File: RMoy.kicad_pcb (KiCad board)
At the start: 2 copper layers, 89 x 54 mm, 21 parts, among them J1 AudioJack3_SwitchTR, J2 AudioJack3_SwitchTR, J3 Jack-DC, U1 OPA2134

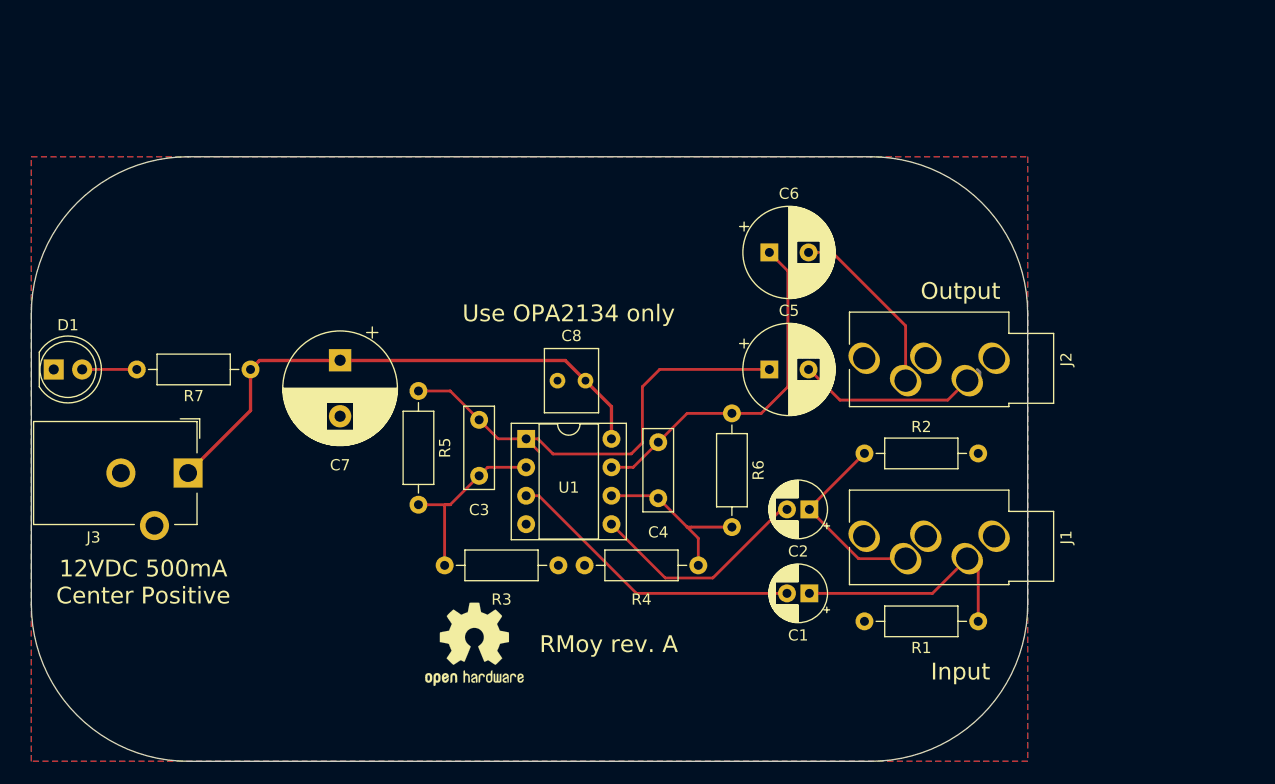
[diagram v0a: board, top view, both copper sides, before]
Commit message: PCB is reworked
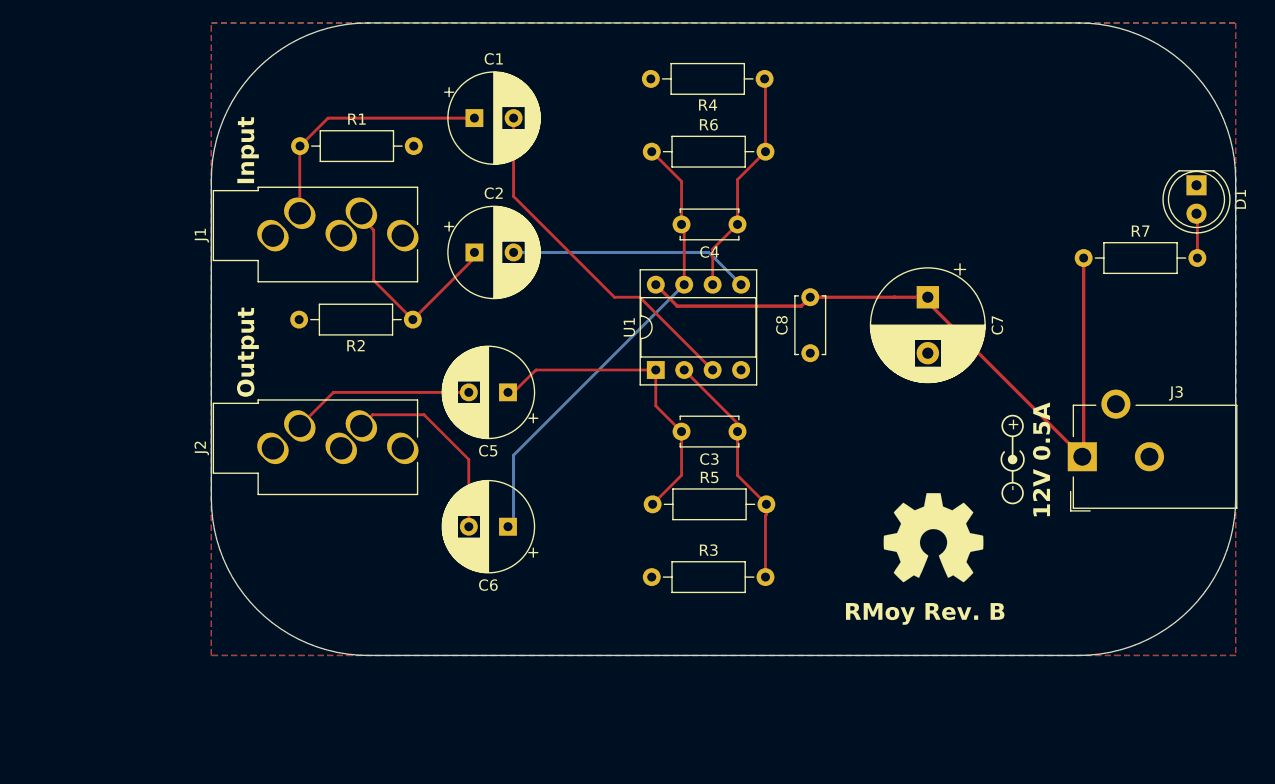
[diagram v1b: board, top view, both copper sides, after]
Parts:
- removed the REF** at (136.0, 109.0)
- added REF**: Symbol_Barrel_Polarity, Symbol:Symbol_Barrel_Polarity, F.Cu at (184.0, 92.5)
- added REF**: OSHW-Symbol_8.9x8mm_SilkScreen, Symbol:OSHW-Symbol_8.9x8mm_SilkScreen, F.Cu at (177.0, 99.5)
- C1, C2: value 47u -> 100u; footprint Capacitor_THT:CP_Radial_D5.0mm_P2.00mm -> Capacitor_THT:CP_Radial_D8.0mm_P3.50mm
- C3, C4: footprint Capacitor_THT:C_Rect_L7.2mm_W2.5mm_P5.00mm_FKS2_FKP2_MKS2_MKP2 -> Capacitor_THT:C_Disc_D5.0mm_W2.5mm_P5.00mm
- C7: value 330u -> 470u
- C8: value 1u -> 100n; footprint Capacitor_THT:C_Rect_L4.6mm_W5.5mm_P2.50mm_MKS02_FKP02 -> Capacitor_THT:C_Disc_D5.0mm_W2.5mm_P5.00mm
- R5, R6: value 1K5 -> 680
- moved D1 103.4 mm to (200.5, 68.0), turned to -90 degrees
- moved J3 79.9 mm to (190.3, 92.2), turned to 90 degrees
- moved R7 75.1 mm to (190.4, 74.5), turned to 0 degrees
- moved R1 74.0 mm to (120.4, 64.5), turned to 0 degrees
- moved J1 69.8 mm to (118.0, 72.5), turned to 90 degrees
- moved J2 64.9 mm to (118.0, 91.5), turned to 90 degrees
- moved C7 52.8 mm to (176.5, 78.0)
- moved C1 51.9 mm to (136.0, 62.0), turned to 0 degrees
- moved R4 43.9 mm to (161.9, 58.5)
- moved R2 42.1 mm to (130.5, 80.0), turned to 180 degrees
- moved C2 37.7 mm to (136.0, 74.0), turned to 0 degrees
- moved C6 33.8 mm to (139.0, 98.5), turned to 180 degrees
- moved C4 25.5 mm to (159.5, 71.5), turned to 180 degrees
- moved R6 24.4 mm to (151.8, 65.0), turned to 0 degrees
- moved C5 23.4 mm to (139.0, 86.5), turned to 180 degrees
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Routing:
- net +12V: track 48.7 -> 62.7 mm
- net Net-(C3-Pad2): track 41.3 -> 28.0 mm
- net Net-(C4-Pad2): track 31.4 -> 41.5 mm
- net Net-(U1A-+): track 26.4 -> 31.2 mm
- net Net-(U1A--): track 16.9 -> 21.6 mm
- net Net-(U1B--): track 15.8 -> 20.4 mm
- net Net-(C2-Pad1): track 17.5 -> 19.7 mm
- net Net-(U1B-+): track 19.7 -> 21.5 mm
- net Net-(C6-Pad2): track 16.3 -> 17.7 mm
- net Net-(C1-Pad1): track 21.4 -> 22.7 mm
- net Net-(D1-A): track 4.88 -> 3.99 mm
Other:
- board size 89 x 54 mm -> 91.5 x 56.5 mm
- board text added: "+"
- board text added: "-"
- board text added: "12V 0.5A"
- board text added: "RMoy Rev. B"
- board text removed: "12VDC 500mA Center Positive"
- board text removed: "RMoy rev. A"
- board text removed: "Use OPA2134 only"
